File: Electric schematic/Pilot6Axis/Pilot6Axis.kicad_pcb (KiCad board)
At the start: 2 copper layers, 75.8 x 53.8 mm, 63 parts, among them IC1 ESP32-WROOM-32U, IC2 LM27313XMFX_NOPB, J1 BTN1, J10 Power switch, J11 TP4056, J12 OLED, J13 USB_C_Receptacle_USB2.0_16P, J14 BTN9, J15 BTN11, J16 BTN10, J2 BTN2, J3 BTN3, J4 BTN4, J5 BTN5, J6 BTN6, J7 BTN7, J8 BTN8, J9 BAT, Q1 Q_NPN_EBC, Q2 Q_NPN_EBC, SW1 SW_Push, SW2 SW_Push, U1 JOYSTICK1, U2 JOYSTICK2, U3 AMS1117-3.3, U4 USBLC6-2SC6, U5 CP2102N-Axx-xQFN28

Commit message: Update pilot PCB versin 1.0
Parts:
- removed IC2: LM27313XMFX_NOPB, KLM27313XMF_NOPB:SOT95P280X145-5N
- removed J4: BTN4, molex-2pin:HDRV2W64P254_1X2_580X508X1170P
- removed Q2: Q_NPN_EBC, S8050:SOT95P240X115-3N
- removed U5: CP2102N-Axx-xQFN28, Package_DFN_QFN:QFN-28-1EP_5x5mm_P0.5mm_EP3.35x3.35mm
- added C16: 10uF, Capacitor_SMD:C_0603_1608Metric, F.Cu at (180.6, 114.5)
- added J17: TP4056, Package_SO:SOP-8-1EP_4.57x4.57mm_P1.27mm_EP4.57x4.45mm, F.Cu at (169.9, 115.6)
- added J18: BAT, Connector_Molex:Molex_KK-254_AE-6410-02A_1x02_P2.54mm_Vertical, F.Cu at (169.5, 121.7)
- added J19: Conn_02x03_Odd_Even, Connector_PinSocket_2.54mm:PinSocket_2x03_P2.54mm_Vertical, F.Cu at (132.8, 89.8)
- added Q3: S9014, PCM_JLCPCB:Q_SOT-23, F.Cu at (124.0, 110.9)
- added R13: 470R, Resistor_SMD:R_0603_1608Metric, F.Cu at (123.6, 116.7)
- added R14: 470R, Resistor_SMD:R_0603_1608Metric, F.Cu at (123.5, 100.9)
- added R20: 4k7, Resistor_SMD:R_0402_1005Metric, F.Cu at (156.1, 93.4)
- added R21: 1k, Resistor_SMD:R_0603_1608Metric, F.Cu at (178.9, 117.6)
- added R22: 1k, Resistor_SMD:R_0603_1608Metric, F.Cu at (177.3, 117.6)
- added R23: 0.2, Resistor_SMD:R_1206_3216Metric, F.Cu at (160.1, 112.6)
- C1: value 2.2uF -> 4.7uF
- C10: value 10uF -> 100n
- C11: value 0.1uF -> 100n
- C12: value 1nF -> 10u; footprint Capacitor_SMD:C_0603_1608Metric -> Resistor_SMD:R_0603_1608Metric
- C14, C15: value 100nF -> 1nF
- C2: value 4.7uF -> 220pF
- C3: value 220pF -> 2.2uF
- C4: value 1nF -> 100nF
- C6: value 10uF -> 1nF
- C7: value 10nF -> 100nF; footprint Resistor_SMD:R_0603_1608Metric -> Capacitor_SMD:C_0603_1608Metric
- C8: value 10uF -> 10nF
- C9: value 0.1uF -> 4.7u
- IC1: value ESP32-WROOM-32U -> LM27313XMFX_NOPB; footprint ESP32-WROOM-32U:ESP32WROOM32D -> Package_TO_SOT_SMD:SOT-23-5
- J1: value BTN1 -> Power switch; footprint molex-2pin:HDRV2W64P254_1X2_580X508X1170P -> Connector_Molex:Molex_KK-254_AE-6410-02A_1x02_P2.54mm_Vertical
- J10: value Power switch -> BTN5; footprint molex-2pin:HDRV2W64P254_1X2_580X508X1170P -> Connector_Molex:Molex_KK-254_AE-6410-02A_1x02_P2.54mm_Vertical
- J11: value TP4056 -> BTN6; footprint TP4056:SOIC127P600X175-9N -> Connector_Molex:Molex_KK-254_AE-6410-02A_1x02_P2.54mm_Vertical
- J12: value OLED -> BTN7; footprint molex-4pin:MOLEX_22232041 -> Connector_Molex:Molex_KK-254_AE-6410-02A_1x02_P2.54mm_Vertical
- J13: value USB_C_Receptacle_USB2.0_16P -> BTN8; footprint Connector_USB:USB_C_Receptacle_HCTL_HC-TYPE-C-16P-01A -> Connector_Molex:Molex_KK-254_AE-6410-02A_1x02_P2.54mm_Vertical
- J14: footprint molex-2pin:HDRV2W64P254_1X2_580X508X1170P -> Connector_Molex:Molex_KK-254_AE-6410-02A_1x02_P2.54mm_Vertical
- J15: value BTN11 -> BTN10; footprint molex-2pin:HDRV2W64P254_1X2_580X508X1170P -> Connector_Molex:Molex_KK-254_AE-6410-02A_1x02_P2.54mm_Vertical
- J16: value BTN10 -> BTN11; footprint molex-2pin:HDRV2W64P254_1X2_580X508X1170P -> Connector_Molex:Molex_KK-254_AE-6410-02A_1x02_P2.54mm_Vertical
- J2: value BTN2 -> USB_C_Receptacle_USB2.0_16P; footprint molex-2pin:HDRV2W64P254_1X2_580X508X1170P -> Connector_USB:USB_C_Receptacle_HCTL_HC-TYPE-C-16P-01A
- J3: value BTN3 -> Conn_02x03_Odd_Even; footprint molex-2pin:HDRV2W64P254_1X2_580X508X1170P -> Connector_PinSocket_2.54mm:PinSocket_2x03_P2.54mm_Vertical
- J5: value BTN5 -> Oled; footprint molex-2pin:HDRV2W64P254_1X2_580X508X1170P -> Connector_PinSocket_2.54mm:PinSocket_2x02_P2.54mm_Vertical
- J6: value BTN6 -> BTN1; footprint molex-2pin:HDRV2W64P254_1X2_580X508X1170P -> Connector_Molex:Molex_KK-254_AE-6410-02A_1x02_P2.54mm_Vertical
- J7: value BTN7 -> BTN2; footprint molex-2pin:HDRV2W64P254_1X2_580X508X1170P -> Connector_Molex:Molex_KK-254_AE-6410-02A_1x02_P2.54mm_Vertical
- J8: value BTN8 -> BTN3; footprint molex-2pin:HDRV2W64P254_1X2_580X508X1170P -> Connector_Molex:Molex_KK-254_AE-6410-02A_1x02_P2.54mm_Vertical
- J9: value BAT -> BTN4; footprint molex-2pin:HDRV2W64P254_1X2_580X508X1170P -> Connector_Molex:Molex_KK-254_AE-6410-02A_1x02_P2.54mm_Vertical
- L1: footprint Inductor_SMD:L_APV_ANR4010 -> Inductor_SMD:L_Cenker_CKCS4018
- Q1: value Q_NPN_EBC -> S9014; footprint S8050:SOT95P240X115-3N -> PCM_JLCPCB:Q_SOT-23
- R10: value 5k1 -> 1k
- R11: value 33k -> 13.3k
- R12: value 1k -> 13.3k
- R15: value 470R -> 13.3k
- R17: value 13.3k -> 1.5k; footprint Resistor_SMD:R_0603_1608Metric -> Resistor_SMD:R_0402_1005Metric
- R18: value 470R -> 1.5k; footprint Resistor_SMD:R_0603_1608Metric -> Resistor_SMD:R_0402_1005Metric
- R19: value 470R -> 4k7; footprint Resistor_SMD:R_0603_1608Metric -> Resistor_SMD:R_0402_1005Metric
- R3: value 1.2k -> 33k
- R4: value 0.5 -> 22R
- R5: value 1k -> 22R
- R6: value 1k -> 5k1
- R7: value 22R -> 5k1
- R8: value 22R -> 22k; footprint Resistor_SMD:R_0603_1608Metric -> Resistor_SMD:R_0402_1005Metric
- R9: value 5k1 -> 43k; footprint Resistor_SMD:R_0603_1608Metric -> Resistor_SMD:R_0402_1005Metric
- SW1, SW2: footprint TS-1088R-02026:TS1088R02026 -> parts:TS1088R02026
- U1: value JOYSTICK1 -> AMS1117-3.3; footprint molex-6pin:MOLEX_22-27-2061 -> Package_TO_SOT_SMD:SOT-223-3_TabPin2
- U2: value JOYSTICK2 -> USBLC6-2SC6; footprint molex-6pin:MOLEX_22-27-2061 -> Package_TO_SOT_SMD:SOT-23-6
- U3: value AMS1117-3.3 -> CP2102N-Axx-xQFN28; footprint Package_TO_SOT_SMD:SOT-223-3_TabPin2 -> Package_DFN_QFN:QFN-28-1EP_5x5mm_P0.5mm_EP3.35x3.35mm
- U4: value USBLC6-2SC6 -> ESP32-WROOM-32U; footprint Package_TO_SOT_SMD:SOT-23-6 -> RF_Module:ESP32-WROOM-32U
- moved J3 56.8 mm to (124.2, 89.9), turned to 180 degrees
- moved U1 55.7 mm to (183.9, 107.5), turned to -90 degrees
- moved C15 47.5 mm to (123.6, 115.1)
- moved R18 46.4 mm to (163.5, 116.9)
- moved J14 45.8 mm to (140.6, 79.9), turned to 0 degrees
- moved J15 44.3 mm to (140.6, 86.8), turned to 0 degrees
- moved J6 44.1 mm to (146.8, 86.8), turned to 0 degrees
- moved J9 43.8 mm to (159.1, 79.9)
- moved IC1 43.8 mm to (171.6, 104.9), turned to 180 degrees
- moved J13 41.3 mm to (171.5, 86.8)
- moved J16 38.4 mm to (146.8, 79.9), turned to 0 degrees
- moved C14 38.3 mm to (125.9, 101.4)
- moved J5 37.1 mm to (153.2, 95.6), turned to 0 degrees
- moved J8 36.5 mm to (153.0, 79.9), turned to 0 degrees
- moved J7 35.9 mm to (153.0, 86.8), turned to 0 degrees
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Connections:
- C1 pad 1: Net-(IC2-VIN) -> +5V
- C10 pad 1: VCC -> /CHARGER/VBUS
- C11 pad 1: VCC -> /USB/3.3V_USB
- C12 pad 1: GND -> /USB/3.3V_USB
- C12 pad 2: Net-(C12-Pad2) -> GND
- C13 pad 1: GND -> Net-(C13-Pad1)
- C13 pad 2: Net-(C13-Pad2) -> GND
- C14 pad 1: +5V -> GND
- C14 pad 2: GND -> Net-(C14-Pad2)
- C15 pad 1: +3.3V -> /MCU/EN
- C2 pad 1: +5V -> Net-(IC1-FB)
- C2 pad 2: GND -> +5V
- C3 pad 1: Net-(IC2-FB) -> /Power/BAT+
- C3 pad 2: +5V -> GND
- C4 pad 1: +3.3V -> +5V
- C6 pad 1: GND -> +3.3V
- C6 pad 2: Net-(D2-A) -> GND
- C7 pad 1: Net-(J13-SHIELD) -> +3.3V
- C8 pad 1: +3.3V -> Net-(J2-SHIELD)
- C9 pad 1: +3.3V -> /CHARGER/VBUS
- D2 pad 2: Net-(D2-A) -> /CHARGER/VCC4
- D3 pad 2: Net-(D2-A) -> /CHARGER/VCC4
- IC1 pad 1: GND -> Net-(D1-A)
- IC1 pad 2: +3.3V -> GND
- IC1 pad 3: /EN -> Net-(IC1-FB)
- IC1 pad 4: /JOYSTICK2_Z -> /Power/BAT+
- IC1 pad 5: /JOYSTICK2_Y -> /Power/BAT+
- J1 pad 1: /BTN1 -> /CHARGER/BAT+
- J1 pad 2: GND -> /Power/BAT+
- J10 pad 1: /BAT+ -> /MCU/BTN5
- J10 pad 2: Net-(IC2-VIN) -> GND
- J11 pad 1: GND -> /MCU/BTN6
- J11 pad 2: Net-(J11-PROG2) -> GND
- J12 pad 1: /SDA -> /MCU/BTN7
- J12 pad 2: /SCL -> GND
- J14 pad 1: /BTN9 -> /MCU/BTN9
- J15 pad 1: /BTN11 -> /MCU/BTN10
- J16 pad 1: /BTN10 -> /MCU/BTN11
- J3 pad 1: /BTN3 -> /MCU/JOYSTICK2_BTN
- J3 pad 2: GND -> /MCU/JOYSTICK2_Z
- J5 pad 1: /BTN5 -> /MCU/SCL
- J5 pad 2: GND -> /MCU/SDA
- J6 pad 1: /BTN6 -> /MCU/BTN1
- J7 pad 1: /BTN7 -> /MCU/BTN2
- J8 pad 1: /BTN8 -> /MCU/BTN3
- J9 pad 1: /BAT+ -> /MCU/BTN4
- L1 pad 2: Net-(IC2-VIN) -> /Power/BAT+
- Q1 pad 1: /RST -> Net-(Q1-B)
- Q1 pad 2: Net-(Q1-B) -> /MCU/IO0
- Q1 pad 3: /EN -> /USB/DTR
- R1 pad 2: Net-(IC2-FB) -> Net-(IC1-FB)
- R10 pad 1: Net-(J13-CC1) -> /USB/3.3V_USB
- R10 pad 2: GND -> Net-(U3-~{RST})
- R11 pad 1: Net-(J13-SHIELD) -> /USB/DTR
- R11 pad 2: GND -> Net-(Q3-B)
- R12 pad 1: +3.3V -> /USB/RTS
- R12 pad 2: Net-(U5-~{RST}) -> Net-(Q1-B)
- R15 pad 1: Net-(U5-TXD) -> /MCU/EN
- R15 pad 2: /TXD -> +3.3V
- R16 pad 1: /DTR -> /MCU/IO0
- R16 pad 2: Net-(Q1-B) -> +3.3V
- R17 pad 1: /RST -> /CHARGER/PROG2
- R17 pad 2: Net-(Q2-B) -> Net-(R17-Pad2)
- R18 pad 1: Net-(C12-Pad2) -> Net-(R17-Pad2)
- R18 pad 2: /IO0 -> GND
- R19 pad 1: Net-(C13-Pad2) -> /MCU/SDA
- R19 pad 2: /EN -> +3.3V
- R2 pad 2: Net-(IC2-FB) -> Net-(IC1-FB)
- R3 pad 1: Net-(J11-PROG2) -> Net-(J2-SHIELD)
- R4 pad 1: VCC -> /USB/USB_CONN_D-
- R4 pad 2: Net-(D2-A) -> /USB/D+
- R5 pad 1: Net-(D3-K) -> /USB/USB_CONN_D+
- R5 pad 2: Net-(J11-~{CHRG}) -> /USB/D-
- R6 pad 1: Net-(D2-K) -> Net-(J2-CC2)
- R6 pad 2: Net-(J11-~{STDBY}) -> GND
- R7 pad 1: Net-(R7-Pad1) -> Net-(J2-CC1)
- R7 pad 2: /D+ -> GND
- R8 pad 1: Net-(R8-Pad1) -> Net-(U3-VBUS)
- R8 pad 2: /D- -> /CHARGER/VBUS
- R9 pad 1: Net-(J13-CC2) -> GND
- R9 pad 2: GND -> Net-(U3-VBUS)
- SW1 pad 2: Net-(C12-Pad2) -> Net-(C13-Pad1)
- SW2 pad 2: Net-(C13-Pad2) -> Net-(C14-Pad2)
- U1 pad 1: /JOYSTICK1_X -> GND
- U1 pad 2: /JOYSTICK1_Y -> +3.3V
- U1 pad 3: /JOYSTICK1_Z -> +5V
- U2 pad 1: /JOYSTICK2_X -> /USB/USB_CONN_D-
- U2 pad 2: /JOYSTICK2_Y -> GND
- U2 pad 3: /JOYSTICK2_Z -> /USB/USB_CONN_D+
- U2 pad 4: /JOYSTICK2_BTN -> /USB/USB_CONN_D+
- U2 pad 5: GND -> /CHARGER/VBUS
- U2 pad 6: +3.3V -> /USB/USB_CONN_D-
- U3 pad 1: GND -> unconnected-(U3-~{DCD}-Pad1)
- U3 pad 2: +3.3V -> unconnected-(U3-~{RI}/CLK-Pad2)
- U3 pad 3: +5V -> GND
- U4 pad 1: Net-(R7-Pad1) -> GND
- U4 pad 2: GND -> +3.3V
- U4 pad 3: Net-(R8-Pad1) -> /MCU/EN
- U4 pad 4: /USB_CONN_D+ -> /MCU/JOYSTICK2_Z
- U4 pad 5: VCC -> /MCU/JOYSTICK2_Y
- U4 pad 6: /USB_CONN_D- -> /MCU/JOYSTICK2_X
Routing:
- net /MCU/JOYSTICK1_BTN: track 0.00 -> 121.1 mm, vias 0 -> 1
- net /MCU/JOYSTICK2_BTN: track 0.00 -> 114.9 mm, vias 0 -> 1
- net /BTN9: track 107.2 -> 0.00 mm, vias 2 -> 0
- net /BTN10: track 100.3 -> 0.00 mm, vias 2 -> 0
- net /BTN11: track 94.9 -> 0.00 mm, vias 2 -> 0
- net /BTN5: track 91.5 -> 0.00 mm, vias 1 -> 0
- net /BTN6: track 87.5 -> 0.00 mm, vias 1 -> 0
- net /BTN7: track 83.5 -> 0.00 mm, vias 1 -> 0
- net /BTN8: track 79.6 -> 0.00 mm, vias 1 -> 0
- net /USB/RTS: track 0.00 -> 62.6 mm, vias 0 -> 2
- net /BTN4: track 62.1 -> 0.00 mm, vias 1 -> 0
- net /BTN1: track 60.2 -> 0.00 mm, vias 2 -> 0
- net /MCU/BTN6: track 0.00 -> 57.7 mm, vias 0 -> 1
- net /MCU/BTN4: track 0.00 -> 55.1 mm, vias 0 -> 1
- net /MCU/BTN8: track 0.00 -> 52.8 mm, vias 0 -> 1
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- added copper zone on F.Cu, net +3.3V
- added copper zone on F.Cu, net +5V
- added copper zone on F.Cu, net /CHARGER/VBUS
- added copper zone on B.Cu, net GND
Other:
- board size 75.8 x 53.8 mm -> 74 x 54 mm
- board text added: "3V3"
- board text added: "B1"
- board text added: "B10"
- board text added: "B11"
- board text added: "B2"
- board text added: "B3"
- board text added: "B4"
- board text added: "B5"
- board text added: "B6"
- board text added: "B7"
- board text added: "B8"
- board text added: "B9"
- board text added: "BAT"
- board text added: "BOOT"
- board text added: "EN"
- board text added: "JOY1"
- board text added: "JOY2"
- board text added: "OLED"
- board text added: "SCL"
- board text added: "SDA"
- board text added: "SW"
- board text added: "VBAT"
- board text added: "X"
- board text added: "Y"
- board text added: "Z"
- board text removed: "+3.3V"
- board text removed: "BAT+"
- board text removed: "IN"
- board text removed: "IN X"
- board text removed: "IN Y"
- board text removed: "IN Z"

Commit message: added rev number and projekct info
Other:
- board text added: "Pilot 6 axis designed by Patryk Dudziński REV1.0 21.02.2025"
- board text added: "QC"
- board text added: "S/N"
- board text added: "github.com/X-Lemon-X/Pilot_6_axis"
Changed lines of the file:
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@@
 		(tags "resistor")
 		(property "Reference" "R20"
-			(at 2.5 0 360)
+			(at 2.5 0 0)
 			(layer "F.SilkS")
 			(effects
@@
 		)
 		(property "Value" "4k7"
-			(at 0 1.17 360)
+			(at 0 1.17 0)
 			(layer "F.Fab")
 			(effects
@@
 		)
 		(fp_text user "${REFERENCE}"
-			(at 0 0 360)
+			(at 0 0 0)
 			(layer "F.Fab")
 			(effects
@@
 		(tags "resistor")
 		(property "Reference" "R19"
-			(at 2.25 0 360)
+			(at 2.25 0 0)
 			(layer "F.SilkS")
 			(effects
@@
 		)
 		(property "Value" "4k7"
-			(at 0 1.17 360)
+			(at 0 1.17 0)
 			(layer "F.Fab")
 			(effects
@@
 		)
 		(fp_text user "${REFERENCE}"
-			(at 0 0 360)
+			(at 0 0 0)
 			(layer "F.Fab")
 			(effects
@@
 	)
 	(gr_line
+		(start 162.7287 101.630801)
+		(end 162.728699 109.1308)
+		(stroke
+			(width 0.2)
+			(type default)
+		)
+		(layer "B.SilkS")
+	)
+	(gr_poly
+		(pts
+			(xy 167.761201 101.6308) (xy 167.7612 109.1308) (xy 157.696199 109.130801) (xy 157.6962 101.630801)
+		)
+		(stroke
+			(width 0.3)
+			(type default)
+		)
+		(fill none)
+		(layer "B.SilkS")
+	)
+	(gr_poly
+		(pts
+			(xy 187.290791 101.6308) (xy 187.290791 109.1308) (xy 167.6962 109.130801) (xy 167.6962 101.630801)
+		)
+		(stroke
+			(width 0.3)
+			(type default)
+		)
+		(fill none)
+		(layer "B.SilkS")
+	)
+	(gr_line
 		(start 187.0612 71.6308)
 		(end 117.0612 71.6308)
@@
 		(layer "Edge.Cuts")
 	)
+	(gr_text "Pilot 6 axis\ndesigned by Patryk Dudziński\nREV1.0    21.02.2025"
+		(at 186.478699 106.9308 0)
+		(layer "B.SilkS")
+		(effects
+			(font
+				(size 0.8 0.8)
+				(thickness 0.2)
+				(bold yes)
+			)
+			(justify left bottom mirror)
+		)
+	)
+	(gr_text "S/N"
+		(at 162.728699 103.030799 -0)
+		(layer "B.SilkS" knockout)
+		(effects
+			(font
+				(size 1 1)
+				(thickness 0.1)
+			)
+			(justify left bottom mirror)
+		)
+	)
+	(gr_text "QC"
+		(at 167.678699 103.0508 -0)
+		(layer "B.SilkS" knockout)
+		(effects
+			(font
+				(size 1 1)
+				(thickness 0.1)
+			)
+			(justify left bottom mirror)
+		)
+	)
+	(gr_text "github.com/X-Lemon-X/Pilot_6_axis"
+		(at 167.7612 73.6308 0)
+		(layer "B.SilkS")
+		(effects
+			(font
+				(size 1 1)
+				(thickness 0.15)
+			)
+			(justify left bottom mirror)
+		)
+	)
 	(gr_text "GND"

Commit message: update schematic to kicajd 9.0,    fixed usb D=/D- wrongly inerconnected , otherwise pcb seems to be woekring
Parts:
- moved R4 2.84 mm to (152.1, 107.6), turned to 0 degrees
- moved R5 1.34 mm to (152.2, 110.0)
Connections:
- R4 pad 2: /USB/D+ -> /USB/D-
- R5 pad 2: /USB/D- -> /USB/D+
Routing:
- net /USB/USB_CONN_D-: track 10.4 -> 14.1 mm
- net /USB/D-: track 3.94 -> 1.76 mm
- net /USB/USB_CONN_D+: track 10.4 -> 11.6 mm
- net /USB/D+: track 3.89 -> 3.24 mm

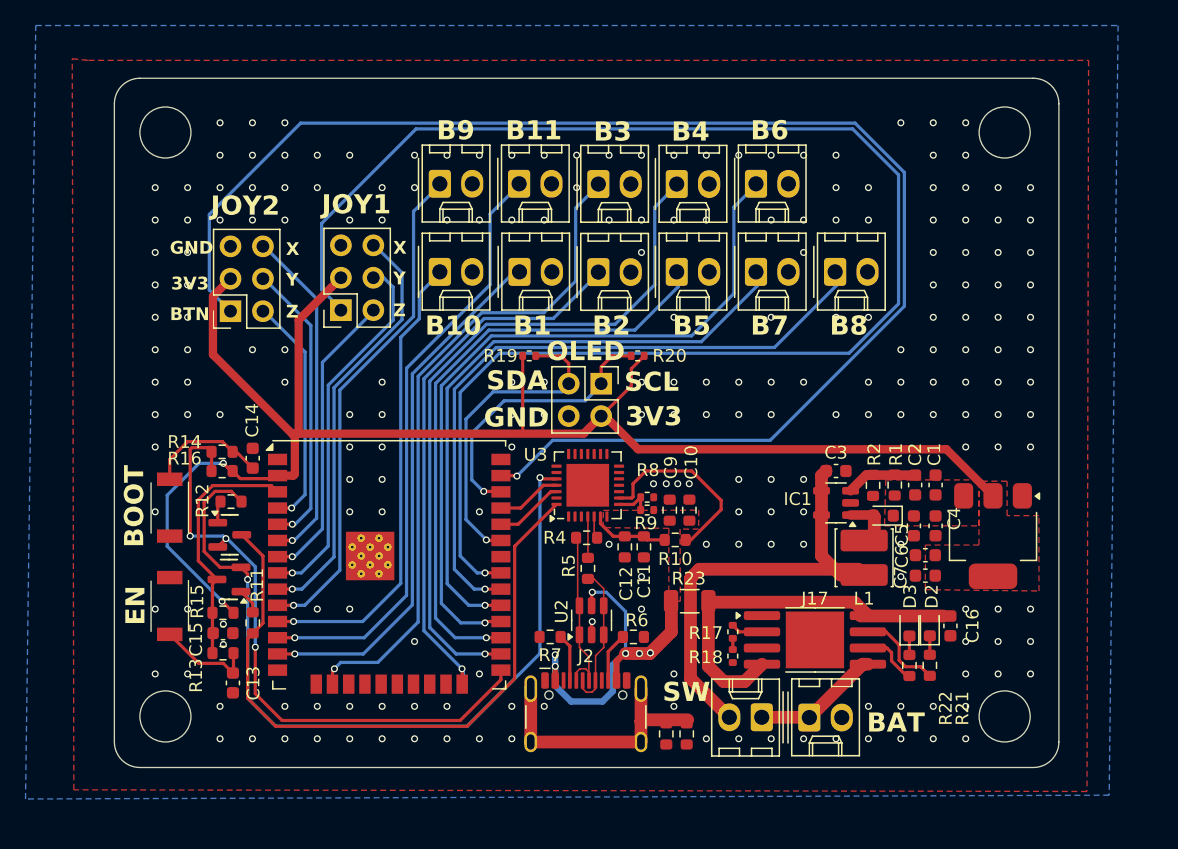
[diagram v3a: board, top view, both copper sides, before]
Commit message: upgrade board to use USB BD for power delivery and addded SPI screen conector
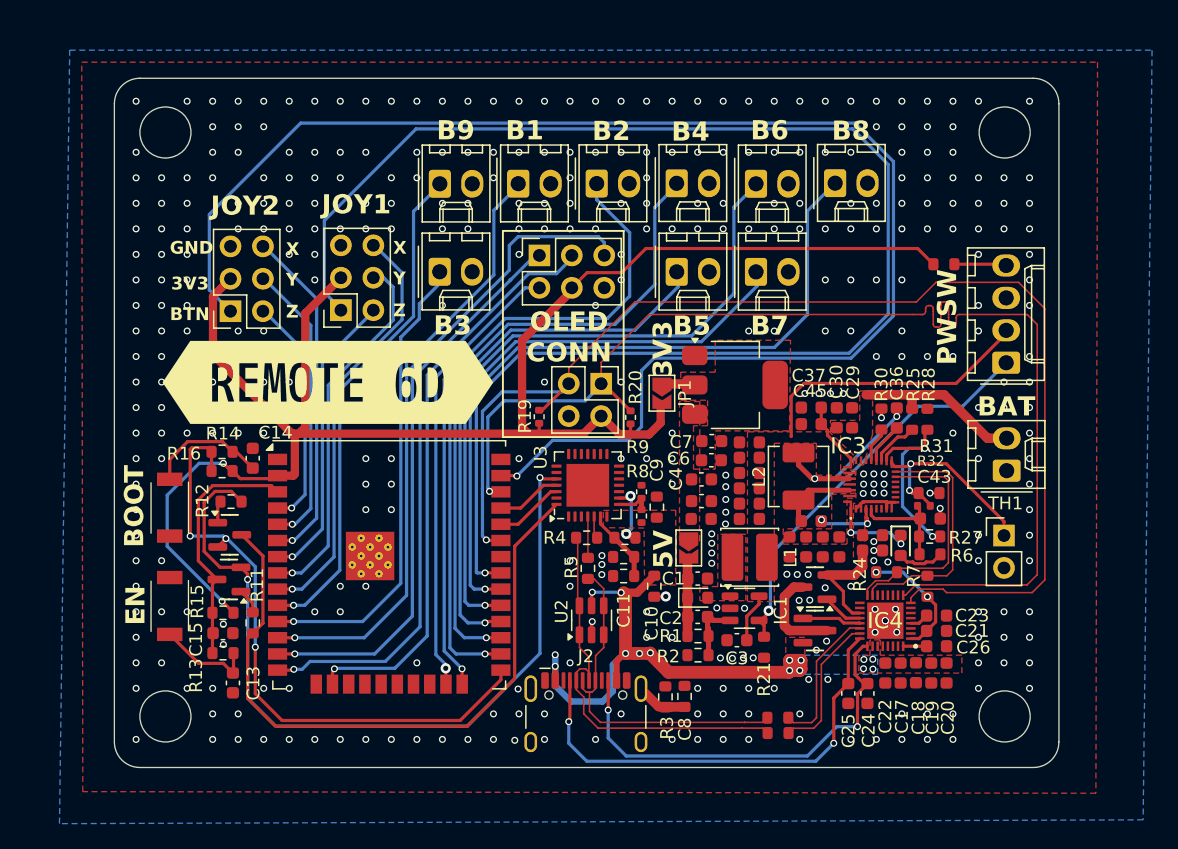
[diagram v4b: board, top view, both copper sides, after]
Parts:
- removed D2, D3: LED, LED_SMD:LED_0603_1608Metric
- removed J17: TP4056, Package_SO:SOP-8-1EP_4.57x4.57mm_P1.27mm_EP4.57x4.45mm
- removed J18: BAT, Connector_Molex:Molex_KK-254_AE-6410-02A_1x02_P2.54mm_Vertical
- removed R23: 0.2, Resistor_SMD:R_1206_3216Metric
- added C17: 4.7uF, PCM_JLCPCB:C_0603, F.Cu at (176.7, 118.2)
- added C18: 100nF, PCM_JLCPCB:C_0603, F.Cu at (177.9, 118.2)
- added C19: 100nF, PCM_JLCPCB:C_0603, F.Cu at (179.1, 118.2)
- added C20: 100nF, PCM_JLCPCB:C_0603, F.Cu at (180.3, 118.2)
- added C21: 10uF, PCM_JLCPCB:C_0603, F.Cu at (179.5, 114.9)
- added C22: 10uF, PCM_JLCPCB:C_0603, F.Cu at (175.5, 118.2)
- added C23: 10uF, PCM_JLCPCB:C_0603, F.Cu at (179.5, 113.7)
- added C24: 220pF, Capacitor_SMD:C_0603_1608Metric, F.Cu at (174.1, 119.8)
- added C25: 220pF, Capacitor_SMD:C_0603_1608Metric, F.Cu at (172.6, 119.8)
- added C26: 100nF, PCM_JLCPCB:C_0603, F.Cu at (179.5, 116.1)
- added C27: 100nF, PCM_JLCPCB:C_0603, F.Cu at (174.5, 107.4)
- added C28: 100nF, PCM_JLCPCB:C_0603, F.Cu at (174.5, 108.6)
- added C29: 10uF, PCM_JLCPCB:C_0603, F.Cu at (172.9, 98.2)
- added C30: 10uF, PCM_JLCPCB:C_0603, F.Cu at (171.7, 98.2)
- added C31: 10uF, PCM_JLCPCB:C_0603, F.Cu at (169.3, 108.4)
- added C32: 10uF, PCM_JLCPCB:C_0603, F.Cu at (168.0, 108.4)
- added C33: 100nF, PCM_JLCPCB:C_0603, F.Cu at (171.9, 108.4)
- added C34: 10uF, PCM_JLCPCB:C_0603, F.Cu at (170.6, 108.4)
- added C35: 47nF, PCM_JLCPCB:C_0603, F.Cu at (169.7, 106.3)
- added C36: 47nF, PCM_JLCPCB:C_0603, F.Cu at (176.4, 98.3)
- added C37: 1nF, PCM_JLCPCB:C_0603, F.Cu at (169.7, 97.4)
- added C38: 10uF, PCM_JLCPCB:C_0603, F.Cu at (164.8, 100.2)
- added C39: 10uF, PCM_JLCPCB:C_0603, F.Cu at (164.8, 106.2)
- added C40: 10uF, PCM_JLCPCB:C_0603, F.Cu at (164.8, 105.0)
- added C41: 10uF, PCM_JLCPCB:C_0603, F.Cu at (164.8, 103.8)
- added C42: 10uF, PCM_JLCPCB:C_0603, F.Cu at (164.8, 102.6)
- added C43: 4.7uF, PCM_JLCPCB:C_0603, F.Cu at (179.0, 106.1)
- added C44: 100nF, PCM_JLCPCB:C_0603, F.Cu at (164.8, 101.4)
- added C45: 1nF, PCM_JLCPCB:C_0603, F.Cu at (169.7, 98.7)
- added D4: Red, PCM_JLCPCB:D_0603, F.Cu at (176.7, 108.2)
- added IC3: BQ25792RQMR, parts:BQ25792RQMR, F.Cu at (174.4, 103.5)
- added IC4: TPS25751SRSMR, parts:QFN40P400X400X100-33N-D, F.Cu at (175.5, 114.1)
- added JP1: SolderJumper_2_Bridged, Jumper:SolderJumper-2_P1.3mm_Open_TrianglePad1.0x1.5mm, F.Cu at (158.0, 96.3)
- added JP300: SolderJumper_2_Bridged, Jumper:SolderJumper-2_P1.3mm_Open_TrianglePad1.0x1.5mm, F.Cu at (160.1, 108.4)
- added L2: 1u, Inductor_SMD:L_APV_APH0420, F.Cu at (168.7, 102.8)
- added Q2: AO3400A, PCM_JLCPCB:Q_SOT-23, F.Cu at (170.0, 114.9)
- added Q4: AO3400A, PCM_JLCPCB:Q_SOT-23, F.Cu at (170.0, 111.5)
- added R24: 4.7kΩ, PCM_JLCPCB:R_0603, F.Cu at (175.6, 110.3)
- added R25: 100Ω, PCM_JLCPCB:R_0603, F.Cu at (177.6, 98.4)
- added R27: 127k, Resistor_SMD:R_0603_1608Metric, F.Cu at (178.9, 107.5)
- added R28: 100kΩ, PCM_JLCPCB:R_0603, F.Cu at (178.8, 98.4)
- added R30: 3kΩ, PCM_JLCPCB:R_0603, F.Cu at (175.2, 98.3)
- added R31: 30kΩ, PCM_JLCPCB:R_0603, F.Cu at (178.9, 104.1)
- added R32: 5.1kΩ, PCM_JLCPCB:R_0402, F.Cu at (178.5, 105.1)
- added TH1: 10k, Connector_PinHeader_2.54mm:PinHeader_1x02_P2.54mm_Vertical, F.Cu at (184.8, 107.5)
- added kibuzzard-6828A41A: G***, kibuzzard-6828A41A, F.Cu at (131.8, 95.5)
- C16: footprint Capacitor_SMD:C_0603_1608Metric -> PCM_JLCPCB:C_0603
- J1: value Power switch -> Battery input
- J15: value BTN10 -> Power switch; footprint Connector_Molex:Molex_KK-254_AE-6410-02A_1x02_P2.54mm_Vertical -> Connector_Molex:Molex_KK-254_AE-6410-04A_1x04_P2.54mm_Vertical
- J16: value BTN11 -> Oled; footprint Connector_Molex:Molex_KK-254_AE-6410-02A_1x02_P2.54mm_Vertical -> Connector_PinSocket_2.54mm:PinSocket_2x03_P2.54mm_Vertical
- R17, R18: value 1.5k -> 22Ω; footprint Resistor_SMD:R_0402_1005Metric -> PCM_JLCPCB:R_0603
- R21: value 1k -> 10kΩ; footprint Resistor_SMD:R_0603_1608Metric -> PCM_JLCPCB:R_0603
- R22: value 1k -> 1kΩ; footprint Resistor_SMD:R_0603_1608Metric -> PCM_JLCPCB:R_0603
- R6: value 5k1 -> 1kΩ; footprint Resistor_SMD:R_0603_1608Metric -> PCM_JLCPCB:R_0603
- R7: value 5k1 -> 4.7kΩ; footprint Resistor_SMD:R_0603_1608Metric -> PCM_JLCPCB:R_0603
- moved J15 44.9 mm to (184.9, 93.9), turned to 90 degrees
- moved R22 31.6 mm to (180.1, 86.2), turned to 0 degrees
- moved R7 29.8 mm to (178.8, 111.4), turned to 90 degrees
- moved J1 27.2 mm to (185.0, 102.4), turned to 90 degrees
- moved R6 24.1 mm to (179.0, 108.9)
- moved U1 23.4 mm to (163.7, 95.7), turned to 0 degrees
- moved C16 21.2 mm to (161.0, 106.2), turned to 0 degrees
- moved C1 20.0 mm to (160.8, 110.8), turned to 0 degrees
- moved C2 19.9 mm to (160.8, 113.8), turned to 180 degrees
- moved C7 19.8 mm to (161.9, 100.1), turned to 0 degrees
- moved R1 19.4 mm to (160.8, 115.3), turned to 0 degrees
- moved R2 19.1 mm to (160.8, 116.8), turned to 0 degrees
- moved C4 18.7 mm to (161.1, 103.1), turned to 0 degrees
- moved C6 18.3 mm to (161.8, 101.6), turned to 0 degrees
- moved C5 16.8 mm to (161.1, 104.8), turned to 0 degrees
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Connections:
- net /CHARGER/VBUS renamed /PD/VBUS
- net Net-(D1-A) renamed /Power/BOOST_SW
- C1 pad 1: +5V -> /Power/+5V_UNPROTEC
- C16 pad 1: GND -> +5V
- C16 pad 2: /CHARGER/VCC4 -> GND
- C2 pad 2: +5V -> /Power/+5V_UNPROTEC
- C3 pad 1: /Power/BAT+ -> /PD/VCC_OUT
- C6 pad 1: +3.3V -> /Power/+3V3_UNPROTEC
- C7 pad 1: +3.3V -> /Power/+3V3_UNPROTEC
- D1 pad 1: +5V -> /Power/+5V_UNPROTEC
- IC1 pad 4: /Power/BAT+ -> /Power/VPOWER_ENABLE
- IC1 pad 5: /Power/BAT+ -> /PD/VCC_OUT
- J1 pad 1: /CHARGER/BAT+ -> GND
- J1 pad 2: /Power/BAT+ -> /BAT+
- J15 pad 1: /MCU/BTN10 -> /Power/VPOWER_ENABLE
- J15 pad 2: GND -> /PD/VCC_OUT
- J16 pad 1: /MCU/BTN11 -> /MCU/MISO
- J16 pad 2: GND -> /MCU/CS
- J2 pad A5: Net-(J2-CC1) -> /PD/CC1
- J2 pad B5: Net-(J2-CC2) -> /PD/CC2
- L1 pad 2: /Power/BAT+ -> /PD/VCC_OUT
- R1 pad 1: +5V -> /Power/+5V_UNPROTEC
- R17 pad 1: /CHARGER/PROG2 -> /USB/USB_CONN_D+
- R17 pad 2: Net-(R17-Pad2) -> /PD/PD_D+
- R18 pad 1: Net-(R17-Pad2) -> /USB/USB_CONN_D-
- R18 pad 2: GND -> /PD/PD_D-
- R21 pad 1: Net-(J17-~{CHRG}) -> /Power/VPOWER_ENABLE
- R21 pad 2: Net-(D2-K) -> GND
- R22 pad 1: Net-(D3-K) -> +3.3V
- R22 pad 2: Net-(J17-~{STDBY}) -> Net-(J15-Pin_4)
- R6 pad 1: Net-(J2-CC2) -> /PD/REGN
- R6 pad 2: GND -> Net-(D4-Pad2)
- R7 pad 1: Net-(J2-CC1) -> /PD/LDO_3V3
- R7 pad 2: GND -> /PD/I2CC_SDA
- U1 pad 2: +3.3V -> /Power/+3V3_UNPROTEC
- U4 pad 11: /MCU/BTN10 -> /MCU/BTN3
- U4 pad 12: /MCU/BTN11 -> /MCU/BTN1
- U4 pad 13: /MCU/BTN1 -> /MCU/MCLK
- U4 pad 14: unconnected-(U4-IO12-Pad14) -> /MCU/MISO
- U4 pad 16: /MCU/BTN3 -> /MCU/MOSI
- U4 pad 23: unconnected-(U4-IO15-Pad23) -> /MCU/CS
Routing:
- net /MCU/SCL: track 22.3 -> 94.8 mm
- net /MCU/SDA: track 25.1 -> 97.5 mm
- net /MCU/MCLK: track 0.00 -> 52.9 mm, vias 0 -> 1
- net /MCU/BTN11: track 47.4 -> 0.00 mm, vias 1 -> 0
- net /MCU/MISO: track 0.00 -> 45.9 mm, vias 0 -> 1
- net /MCU/MOSI: track 0.00 -> 45.5 mm, vias 0 -> 1
- net /Power/BAT+: track 37.0 -> 0.00 mm
- net /MCU/BTN10: track 36.6 -> 0.00 mm, vias 1 -> 0
- net /PD/CC1: track 0.00 -> 35.9 mm, vias 0 -> 2
- net /MCU/CS: track 0.00 -> 35.6 mm, vias 0 -> 1
- net /PD/CC2: track 0.00 -> 33.3 mm, vias 0 -> 2
- net /Power/VPOWER_ENABLE: track 0.00 -> 31.8 mm, vias 0 -> 1
- net /CHARGER/VCC4: track 29.9 -> 0.00 mm
- net /PD/VCC_OUT: track 0.00 -> 26.1 mm
- net /PD/I2CC_SDA: track 0.00 -> 19.3 mm
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- added copper zone on F.Cu, net /BAT+
- added copper zone on F.Cu, net /PD/CHARGER_VSYS
- added copper zone on F.Cu, net /PD/PMID
- added copper zone on B.Cu, net /PD/VBUS
- added copper zone on F.Cu, net /PD/VCC_OUT
- added copper zone on F.Cu, net /Power/+3V3_UNPROTEC
- added copper zone on F.Cu, net /Power/BOOST_SW
- removed copper zone on F.Cu, net +3.3V
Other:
- board text added: "5V"
- board text added: "CL"
- board text added: "CS"
- board text added: "LED"
- board text added: "NTC"
- board text added: "OLED CONN"
- board text added: "PWSW"
- board text added: "Pilot 6 axis designed by Patryk Dudziński REV 2.0 17.05.2025"
- board text added: "SHORT THIS PINS TO POWER ON SYSTEM"
- board text added: "SI"
- board text added: "SO"
- board text added: "VBAT+"
- board text removed: "B10"
- board text removed: "B11"
- board text removed: "OLED"
- board text removed: "Pilot 6 axis designed by Patryk Dudziński REV1.0 21.02.2025"
- board text removed: "SW"
- board text removed: "VBAT"

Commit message: [pcb] cleanup schematics, made power trace slightl less intterfiring with usb
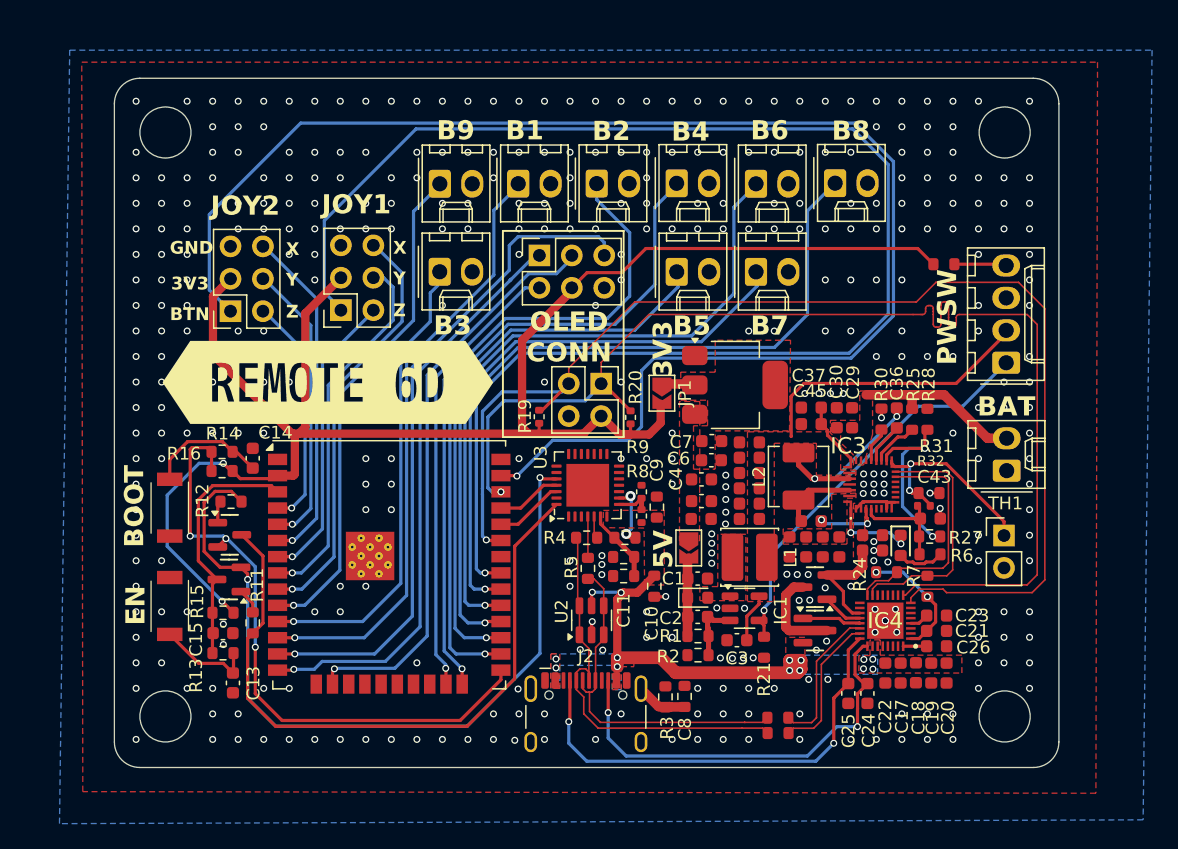
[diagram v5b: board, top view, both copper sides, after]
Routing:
- net /PD/VBUS: track 50.8 -> 31.6 mm, vias 15 -> 14
- net GND: vias 393 -> 394
